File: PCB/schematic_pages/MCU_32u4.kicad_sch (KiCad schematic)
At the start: 1 part, among them U15 ATMEGA32U4-AU

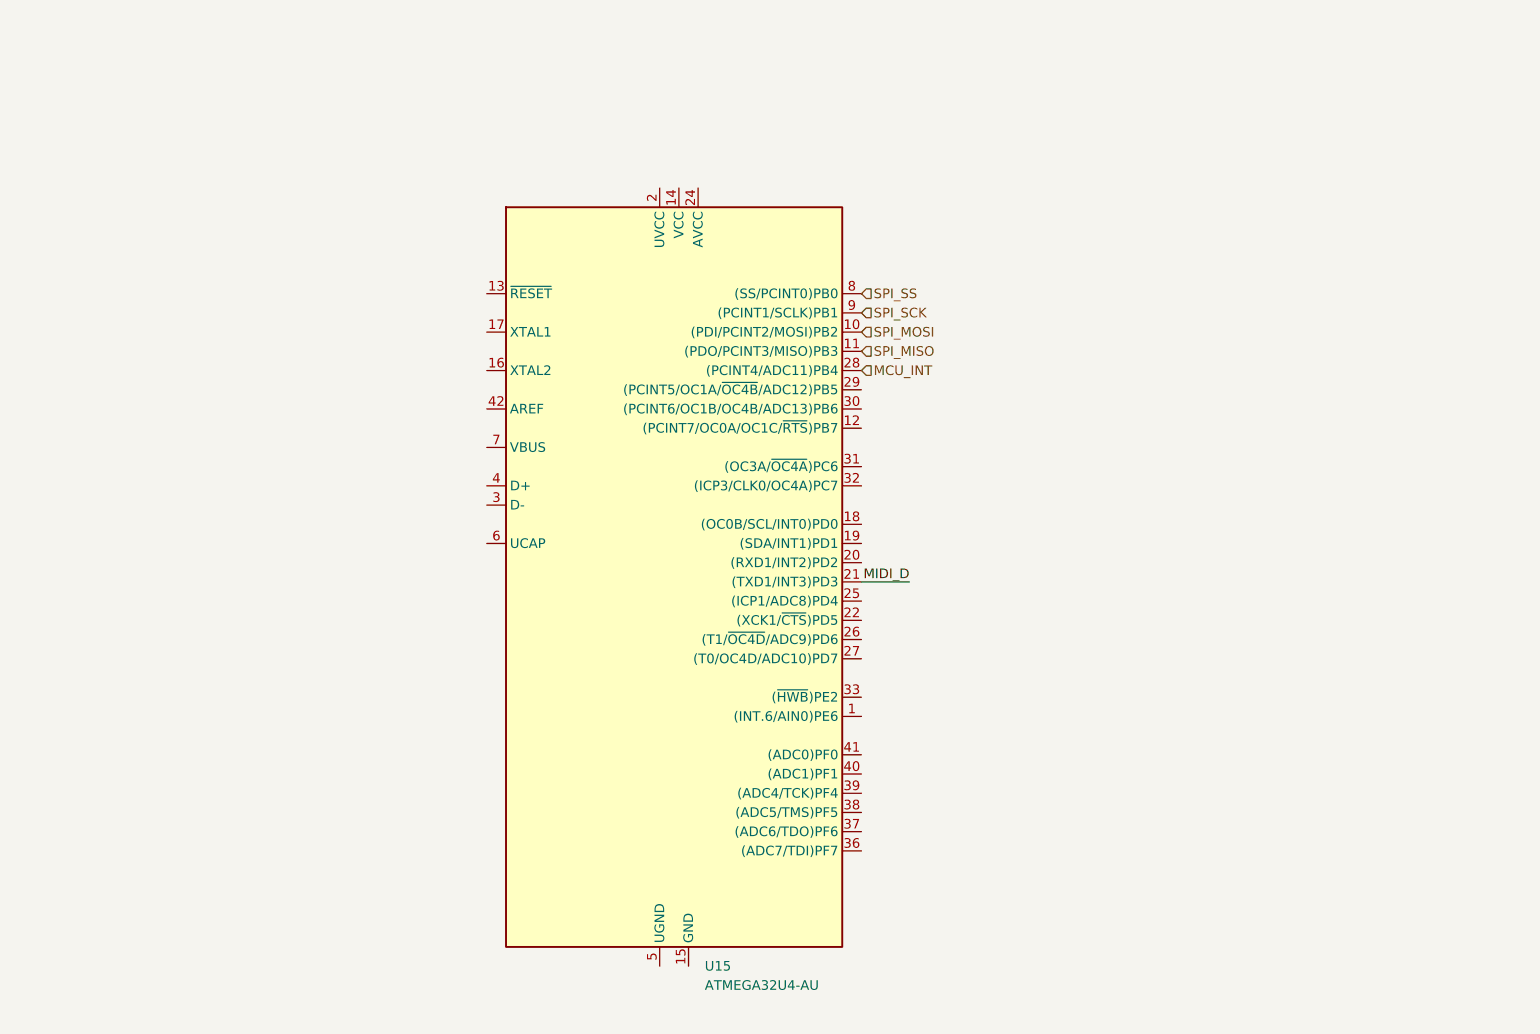
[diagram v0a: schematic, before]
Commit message: USBC & ESD protection
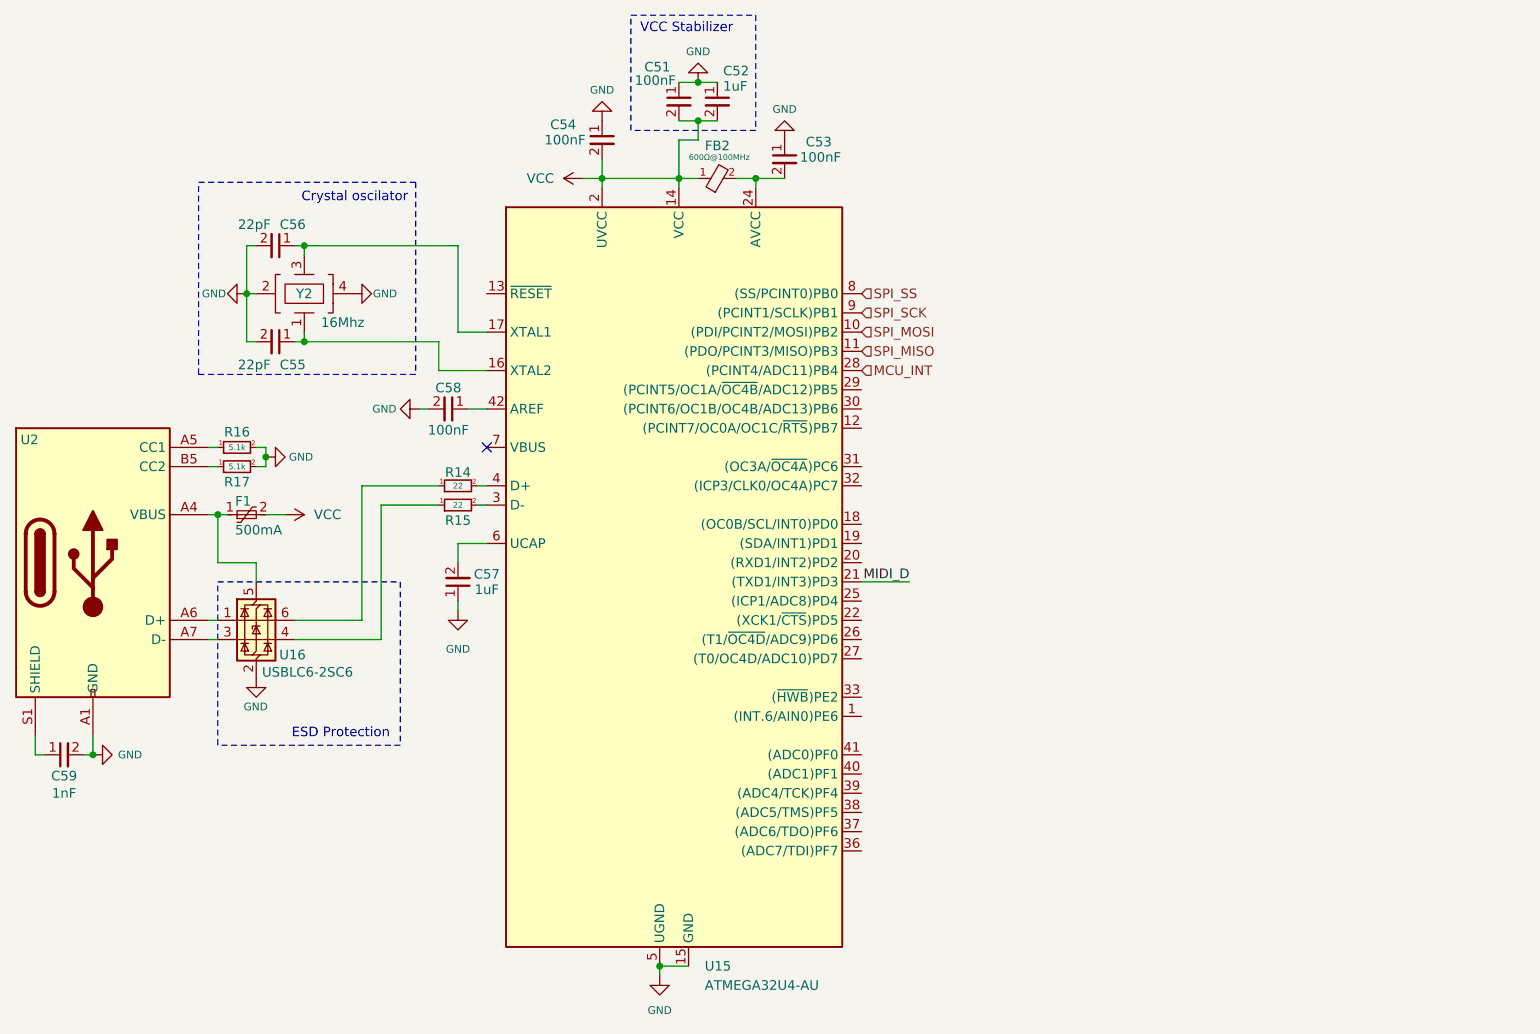
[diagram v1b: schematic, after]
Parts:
- added C51, C53, C54: 100nF, Footprints:0603_C, symbol Symbols:Capacitor 0603
- added C52: 1uF, Footprints:0603_C, symbol Symbols:Capacitor 0603
- added C55, C56: 22pF, Footprints:0603_C, symbol Symbols:Capacitor 0603
- added C57: 1uF, symbol Symbols:Capacitor 0603
- added C58: 100nF, symbol Symbols:Capacitor 0603
- added C59: 1nF, symbol Symbols:Capacitor 0603
- added F1: 500mA, symbol Symbols:Polyfuse
- added FB2: 600Ω@100MHz, symbol Symbols:Ferrite_beat
- added R14, R15: 22, symbol Symbols:Resistor 0603
- added R16, R17: 5.1k, symbol Symbols:Resistor 0603
- added U16: USBLC6-2SC6, symbol Symbols:USBLC6-2SC6
- added U2: ~, symbol Symbols:USB_C_2.0
- added Y2: 16Mhz, Footprints:Crystal Oscillator 16MHz, symbol Symbols:16Mhz_Crystal
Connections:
- net VCC: now reaches U15.14 (VCC), U15.34 (VCC)
- net VCC: now also U15.2 (UVCC), C51.2, C52.2, C54.2, F1.2, FB2.1
- net GND: now reaches U15.15 (GND)
- net GND: now also U15.5 (UGND), C51.1, C52.1, C53.1, C54.1, C55.2, C56.2, C57.1, C58.2, C59.2, R16.2, R17.2, U16.2 (GND), U2.A1 (GND), U2.A12 (GND), U2.B1 (GND), U2.B12 (GND), Y2.2, Y2.4
- net at U15.16 (XTAL2): now also C55.1, Y2.1
- net at U15.17 (XTAL1): now also C56.1, Y2.3
- net at U15.24 (AVCC): now also C53.2, FB2.2; no longer U15.44 (AVCC)
- net at U15.3 (D-): now also R15.2
- net at U15.4 (D+): now also R14.2
- net at U15.42 (AREF): now also C58.1
- net at U15.6 (UCAP): now also C57.2
- new net: F1.1, U16.5 (VBUS), U2.A4 (VBUS)
- new net: U16.1 (I/O1), U2.A6 (D+)
- new net: U16.3 (I/O2), U2.A7 (D-)
- new net: R15.1, U16.4 (I/O2)
- new net: R14.1, U16.6 (I/O1)
- new net: R16.1, U2.A5 (CC1)
- new net: C59.1, U2.S1 (SHIELD)
- new net: R17.1, U2.B5 (CC2)
- no-connect marks 0 -> 1
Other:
- note added: "Crystal oscilator"
- note added: "ESD Protection"
- note added: "VCC Stabilizer"

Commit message: ISP ports, RESET lines, MIDI DIN 5
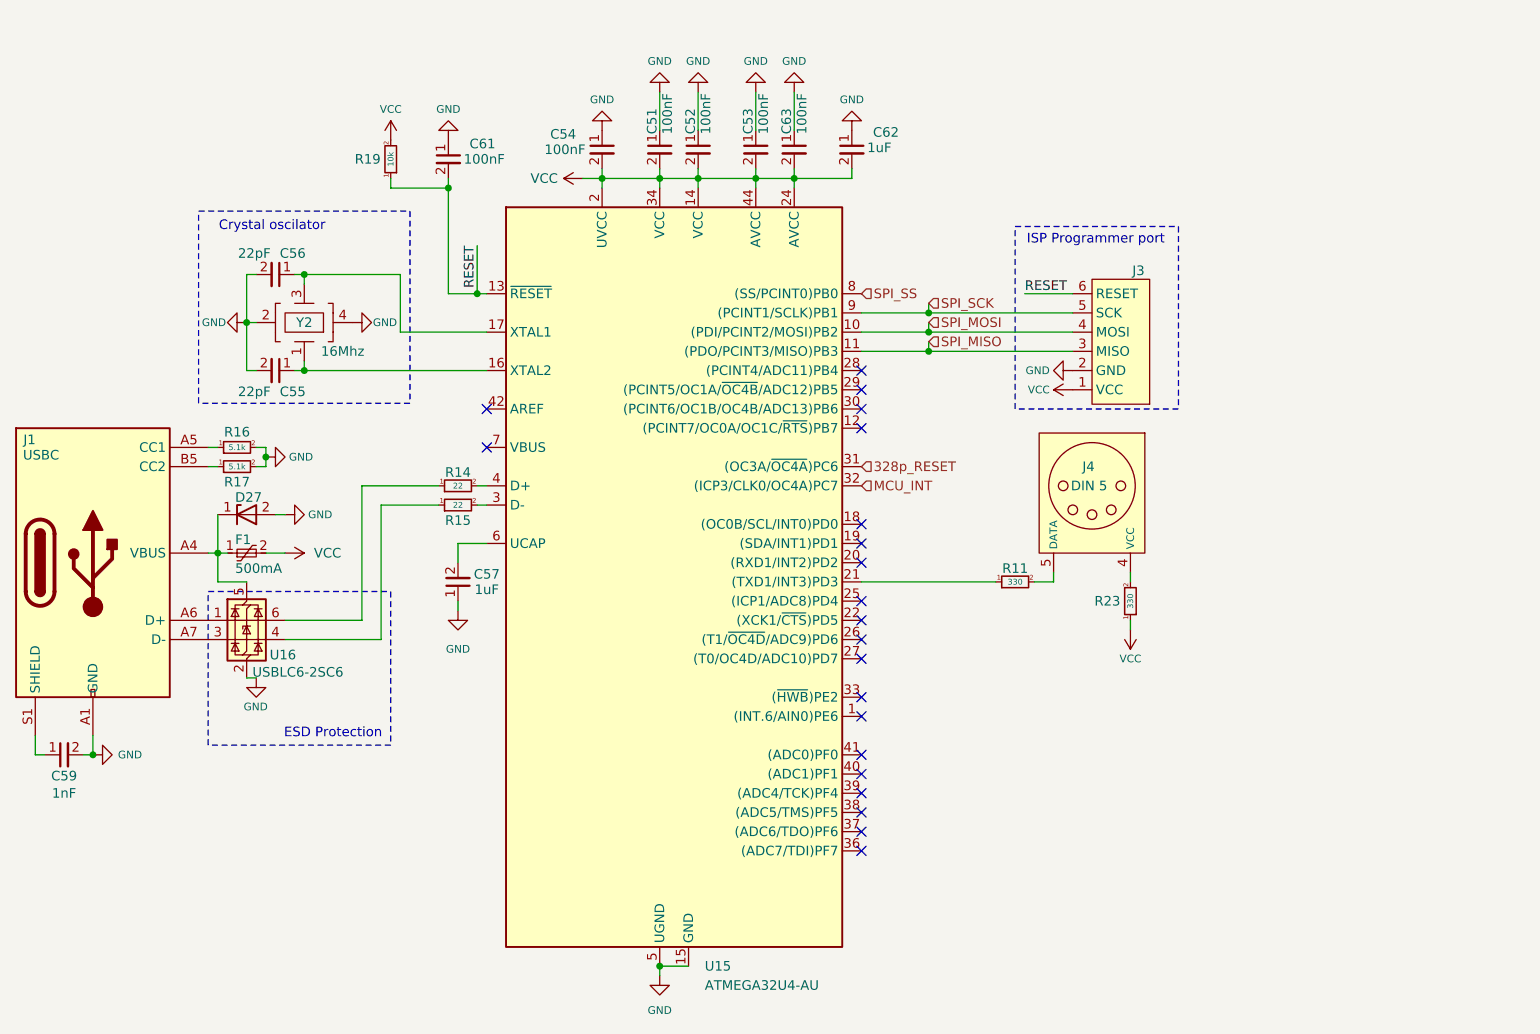
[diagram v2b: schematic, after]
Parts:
- removed C58: 100nF, symbol Symbols:Capacitor 0603
- removed FB2: 600Ω@100MHz, symbol Symbols:Ferrite_beat
- added C61, C63: 100nF, Footprints:0603_C, symbol Symbols:Capacitor 0603
- added C62: 1uF, Footprints:0603_C, symbol Symbols:Capacitor 0603
- added D27: ~, Footprints:TVS Diode SOD-123FL, symbol Symbols:TVS_Diode
- added J3: ~, Footprints:ISP port, symbol Symbols:ISP_Port
- added J4: DIN 5, Footprints:DIN_5 port, symbol Symbols:DIN_5_MIDI
- added R11, R23: 330, Footprints:0603_R, symbol Symbols:Resistor 0603
- added R19: 10k, Footprints:0603_R, symbol Symbols:Resistor 0603
- C52: value 1uF -> 100nF
- C57, C59: footprint (none) -> Footprints:0603_C
- F1: footprint (none) -> Footprints:Resettable Fuse 1206
- J1: renamed from U2; value ~ -> USBC; footprint (none) -> Footprints:USB C Receptacle USB2.0 16PIN
- R14, R15, R16, R17: footprint (none) -> Footprints:0603_R
- U16: footprint (none) -> Footprints:ESD Prot SOT-23-6
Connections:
- net GND: now also C61.1, C62.1, C63.1, D27.2, J3.2 (GND)
- net MCU_INT: now also U15.32 ((ICP3/CLK0/OC4A)PC7); no longer U15.28 ((PCINT4/ADC11)PB4)
- net SPI_MISO: now also J3.3 (MISO)
- net SPI_MOSI: now also J3.4 (MOSI)
- net SPI_SCK: now also J3.5 (SCK)
- net VCC: now also C53.2, U15.24 (AVCC), U15.44 (AVCC), C62.2, C63.2, J3.1 (VCC), R19.2, R23.1
- net at F1.1, J1.A4 (VBUS), U16.5 (VBUS): now also D27.1
- net RESET: now reaches U15.13 (~{RESET})
- net RESET: now also C61.2, J3.6 (RESET), R19.1
- net 328p_RESET: now reaches U15.31 ((OC3A/~{OC4A})PC6)
- net MIDI_D: no longer names the net of U15.21 ((TXD1/INT3)PD3)
- net MIDI_D: now also R11.1
- new net: J4.4 (VCC), R23.2
- new net: J4.5 (DATA), R11.2
- no-connect marks 1 -> 21
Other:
- note added: "ISP Programmer port"
- note removed: "VCC Stabilizer"
- moved on the sheet: C53, C54, C55, C56, F1, U16, Y2

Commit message: pcb: piano done
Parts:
- renumbered C57 to C74, C59 to C75, C62 to C76, C55 to C77, C56 to C78, R14 to R12, R15 to R13, R19 to R15, R23 to R18, R11 to R19, R16 to R8, R17 to R9
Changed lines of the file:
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@@
 		(on_board yes)
 		(dnp no)
-		(property "Reference" "C62"
+		(property "Reference" "C76"
 			(at 131.064 49.784 0)
 			(effects
@@
 			(project "Harmora"
 				(path "/de43e009-b04c-42c1-b131-cdc664039a0d/65694d34-2946-48e5-a5ba-19c1727ab9b1"
-					(reference "C62")
+					(reference "C76")
 					(unit 1)
 				)
@@
 		(on_board yes)
 		(dnp no)
-		(property "Reference" "R23"
+		(property "Reference" "R18"
 			(at 162.052 111.76 0)
 			(effects
@@
 			(project "Harmora"
 				(path "/de43e009-b04c-42c1-b131-cdc664039a0d/65694d34-2946-48e5-a5ba-19c1727ab9b1"
-					(reference "R23")
+					(reference "R18")
 					(unit 1)
 				)
@@
 		(on_board yes)
 		(dnp no)
-		(property "Reference" "C55"
+		(property "Reference" "C77"
 			(at 54.356 84.074 90)
 			(effects
@@
 			(project "Harmora"
 				(path "/de43e009-b04c-42c1-b131-cdc664039a0d/65694d34-2946-48e5-a5ba-19c1727ab9b1"
-					(reference "C55")
+					(reference "C77")
 					(unit 1)
 				)
@@
 		(on_board yes)
 		(dnp no)
-		(property "Reference" "R11"
+		(property "Reference" "R19"
 			(at 149.86 107.442 90)
 			(effects
@@
 			(project ""
 				(path "/de43e009-b04c-42c1-b131-cdc664039a0d/65694d34-2946-48e5-a5ba-19c1727ab9b1"
-					(reference "R11")
+					(reference "R19")
 					(unit 1)
 				)
@@
 		(on_board yes)
 		(dnp no)
-		(property "Reference" "R19"
+		(property "Reference" "R15"
 			(at 64.262 53.34 0)
 			(effects
@@
 			(project "Harmora"
 				(path "/de43e009-b04c-42c1-b131-cdc664039a0d/65694d34-2946-48e5-a5ba-19c1727ab9b1"
-					(reference "R19")
+					(reference "R15")
 					(unit 1)
 				)
@@
 		(on_board yes)
 		(dnp no)
-		(property "Reference" "C56"
+		(property "Reference" "C78"
 			(at 54.356 65.786 90)
 			(effects
@@
 			(project "Harmora"
 				(path "/de43e009-b04c-42c1-b131-cdc664039a0d/65694d34-2946-48e5-a5ba-19c1727ab9b1"
-					(reference "C56")
+					(reference "C78")
 					(unit 1)
 				)
@@
 		(on_board yes)
 		(dnp no)
-		(property "Reference" "R16"
+		(property "Reference" "R8"
 			(at 46.99 89.408 90)
 			(effects
@@
 			(project ""
 				(path "/de43e009-b04c-42c1-b131-cdc664039a0d/65694d34-2946-48e5-a5ba-19c1727ab9b1"
-					(reference "R16")
+					(reference "R8")
 					(unit 1)
 				)
@@
 		(on_board yes)
 		(dnp no)
-		(property "Reference" "R14"
+		(property "Reference" "R12"
 			(at 76.2 94.742 90)
 			(effects
@@
 			(project ""
 				(path "/de43e009-b04c-42c1-b131-cdc664039a0d/65694d34-2946-48e5-a5ba-19c1727ab9b1"
-					(reference "R14")
+					(reference "R12")
 					(unit 1)
 				)
@@
 		(on_board yes)
 		(dnp no)
-		(property "Reference" "R15"
+		(property "Reference" "R13"
 			(at 76.2 101.092 90)
 			(effects
@@
 			(project "Harmora"
 				(path "/de43e009-b04c-42c1-b131-cdc664039a0d/65694d34-2946-48e5-a5ba-19c1727ab9b1"
-					(reference "R15")
+					(reference "R13")
 					(unit 1)
 				)
@@
 		(on_board yes)
 		(dnp no)
-		(property "Reference" "C59"
+		(property "Reference" "C75"
 			(at 24.13 134.874 90)
 			(effects
@@
 			(project ""
 				(path "/de43e009-b04c-42c1-b131-cdc664039a0d/65694d34-2946-48e5-a5ba-19c1727ab9b1"
-					(reference "C59")
+					(reference "C75")
 					(unit 1)
 				)
@@
 		(on_board yes)
 		(dnp no)
-		(property "Reference" "C57"
+		(property "Reference" "C74"
 			(at 80.01 108.204 0)
 			(effects
@@
 			(project ""
 				(path "/de43e009-b04c-42c1-b131-cdc664039a0d/65694d34-2946-48e5-a5ba-19c1727ab9b1"
-					(reference "C57")
+					(reference "C74")
 					(unit 1)
 				)
@@
 		(on_board yes)
 		(dnp no)
-		(property "Reference" "R17"
+		(property "Reference" "R9"
 			(at 46.99 96.012 90)
 			(effects
@@
 			(project "Harmora"
 				(path "/de43e009-b04c-42c1-b131-cdc664039a0d/65694d34-2946-48e5-a5ba-19c1727ab9b1"
-					(reference "R17")
-					(unit 1)
-				)
+					(reference "R9")
+					(unit 1)
+				)

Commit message: PCB V1.0 DONE
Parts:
- removed C54: 100nF, Footprints:0603_C, symbol Symbols:Capacitor 0603
- removed J4: DIN 5, Footprints:DIN_5 port, symbol Symbols:DIN_5_MIDI
- added J4: JST-EH, Footprints:JST-EH port, symbol Symbols:JST-EH
- added R22, R23, R24: 330, Footprints:0603_R, symbol Symbols:Resistor 0603
- renumbered R18 to R20, R19 to R21
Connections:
- net SPI_MISO: now also R24.1; no longer J3.3 (MISO), U15.11 ((PDO/PCINT3/MISO)PB3)
- net SPI_MOSI: now also R23.1; no longer J3.4 (MOSI), U15.10 ((PDI/PCINT2/MOSI)PB2)
- net SPI_SCK: now also R22.1; no longer J3.5 (SCK), U15.9 ((PCINT1/SCLK)PB1)
- net at R20.2: now also J4.1 (VCC)
- net at R21.2: now also J4.2 (DATA)
- net at U16.1 (I/O2): now also J1.A7 (D-); no longer J1.A6 (D+)
- net at U16.3 (I/O1): now also J1.A6 (D+); no longer J1.A7 (D-)
- net at U16.4 (I/O1): now also R12.1; no longer R13.1
- net at U16.6 (I/O2): now also R13.1; no longer R12.1
- new net: J3.3 (MISO), R24.2, U15.11 ((PDO/PCINT3/MISO)PB3)
- new net: J3.4 (MOSI), R23.2, U15.10 ((PDI/PCINT2/MOSI)PB2)
- new net: J3.5 (SCK), R22.2, U15.9 ((PCINT1/SCLK)PB1)
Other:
- moved on the sheet: R20, R21, U16

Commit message: finished reworking pcb
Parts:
- added J5: 128x64 2.42 inc, Footprints:SPI Screen PinHeader, symbol Symbols:SPI_OLED_Display
- added R10, R11: 22, Footprints:0603_R, symbol Symbols:Resistor 0603
- added R16, R18, R25: 10k, Footprints:0603_R, symbol Symbols:Resistor 0603
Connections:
- net 328p_RESET: now also U15.19 ((SDA/INT1)PD1); no longer U15.31 ((OC3A/~{OC4A})PC6)
- net GND: now also J5.1 (GND)
- net MCU_INT: now also U15.20 ((RXD1/INT2)PD2); no longer U15.32 ((ICP3/CLK0/OC4A)PC7)
- net SPI_MOSI: now also J5.4 (SDA/MOSI)
- net SPI_SCK: now also J5.3 (SCK)
- net VCC: now also U15.7 (VBUS), J5.2 (VCC), R16.1, R18.1, R25.2
- net 328P_SS: now reaches U15.18 ((OC0B/SCL/INT0)PD0)
- net DISPLAY_DC: now reaches U15.22 ((XCK1/~{CTS})PD5)
- net DISPLAY_DC: now also J5.6 (DC)
- net DISPLAY_SS: now reaches U15.26 ((T1/~{OC4D}/ADC9)PD6)
- net DISPLAY_SS: now also J5.7 (SS), R18.2
- net DISPLAY_RST: now reaches U15.27 ((T0/OC4D/ADC10)PD7)
- net DISPLAY_RST: now also J5.5 (RES), R16.2
- net SPI_SS: no longer names the net of U15.8 ((SS/PCINT0)PB0)
- net SPI_SS: now also R25.1
- new net SOFT_SPI_CLK: R11.1, U15.32 ((ICP3/CLK0/OC4A)PC7)
- new net SOFT_SPI_MOSI: R10.1, U15.31 ((OC3A/~{OC4A})PC6)
- new net SPI LED chain/SOFT_SPI_CLK: R11.2
- new net SPI LED chain/SOFT_SPI_MOSI: R10.2
- no-connect marks 21 -> 14
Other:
- added sheet SPI LED chain (schematic_pages/SPI_LED_chain.kicad_sch)
- moved on the sheet: C76, R20

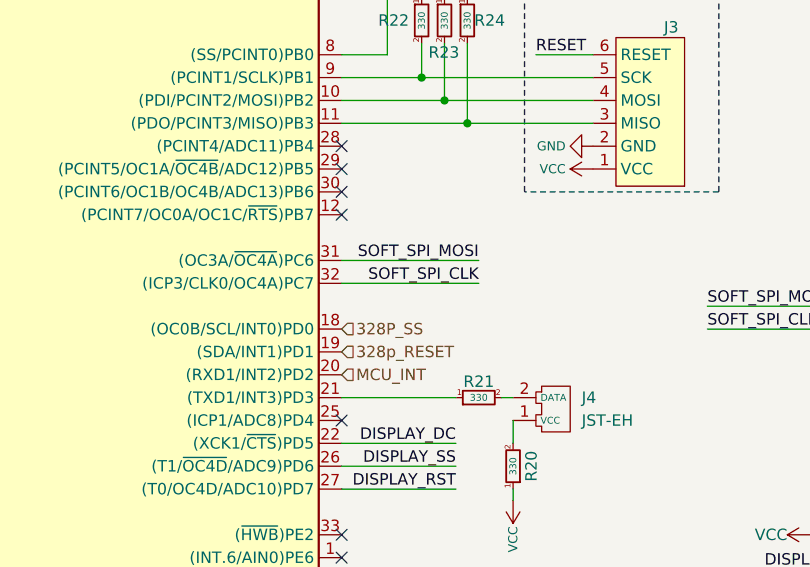
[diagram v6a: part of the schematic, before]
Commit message: MCU_INT to proper pin, VCC to ISP port
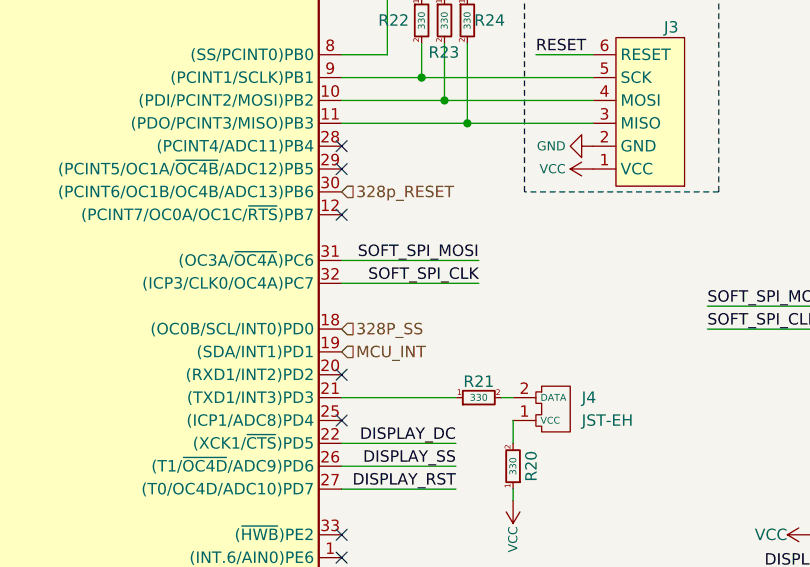
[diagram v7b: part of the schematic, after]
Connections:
- net 328p_RESET: now also U15.30 ((PCINT6/OC1B/OC4B/ADC13)PB6); no longer U15.19 ((SDA/INT1)PD1)
- net MCU_INT: now also U15.19 ((SDA/INT1)PD1); no longer U15.20 ((RXD1/INT2)PD2)
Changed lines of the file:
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@@
-	)
-	(no_connect
-		(at 129.54 86.36)
 	)
 	(no_connect
@@
 	(no_connect
 		(at 129.54 137.16)
+	)
+	(no_connect
+		(at 129.54 106.68)
 	)
 	(no_connect
@@
 	(hierarchical_label "328p_RESET"
 		(shape input)
-		(at 129.54 104.14 0)
+		(at 129.54 86.36 0)
 		(effects
 			(font
@@
 	(hierarchical_label "MCU_INT"
 		(shape input)
-		(at 129.54 106.68 0)
-		(effects
-			(font
+		(at 129.54 104.14 0)
+		(effects
+			(font
